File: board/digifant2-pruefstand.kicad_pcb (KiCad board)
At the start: 2 copper layers, 144 x 150 mm, 78 parts, among them J0 VW ECU HARNESS, J1 12V BENCH IN, J2 IDLE VALVE N71, J3 OLED / UI I2C, Q1 2N7002, Q2 P-MOS -30V >=5A, Q3 2N7002, Q5 2N7002, SW1 PUSH, SW2 PUSH, SW3 PUSH, U1 INA226 (0x40), U2 MCP4728 (0x60), U3 INA226 (0x41), U4 AD9833, U5 Raspberry Pi Pico, U6 TS5A3159A, U7 TS5A3159A, U8 TS5A3159A, Y1 25MHz

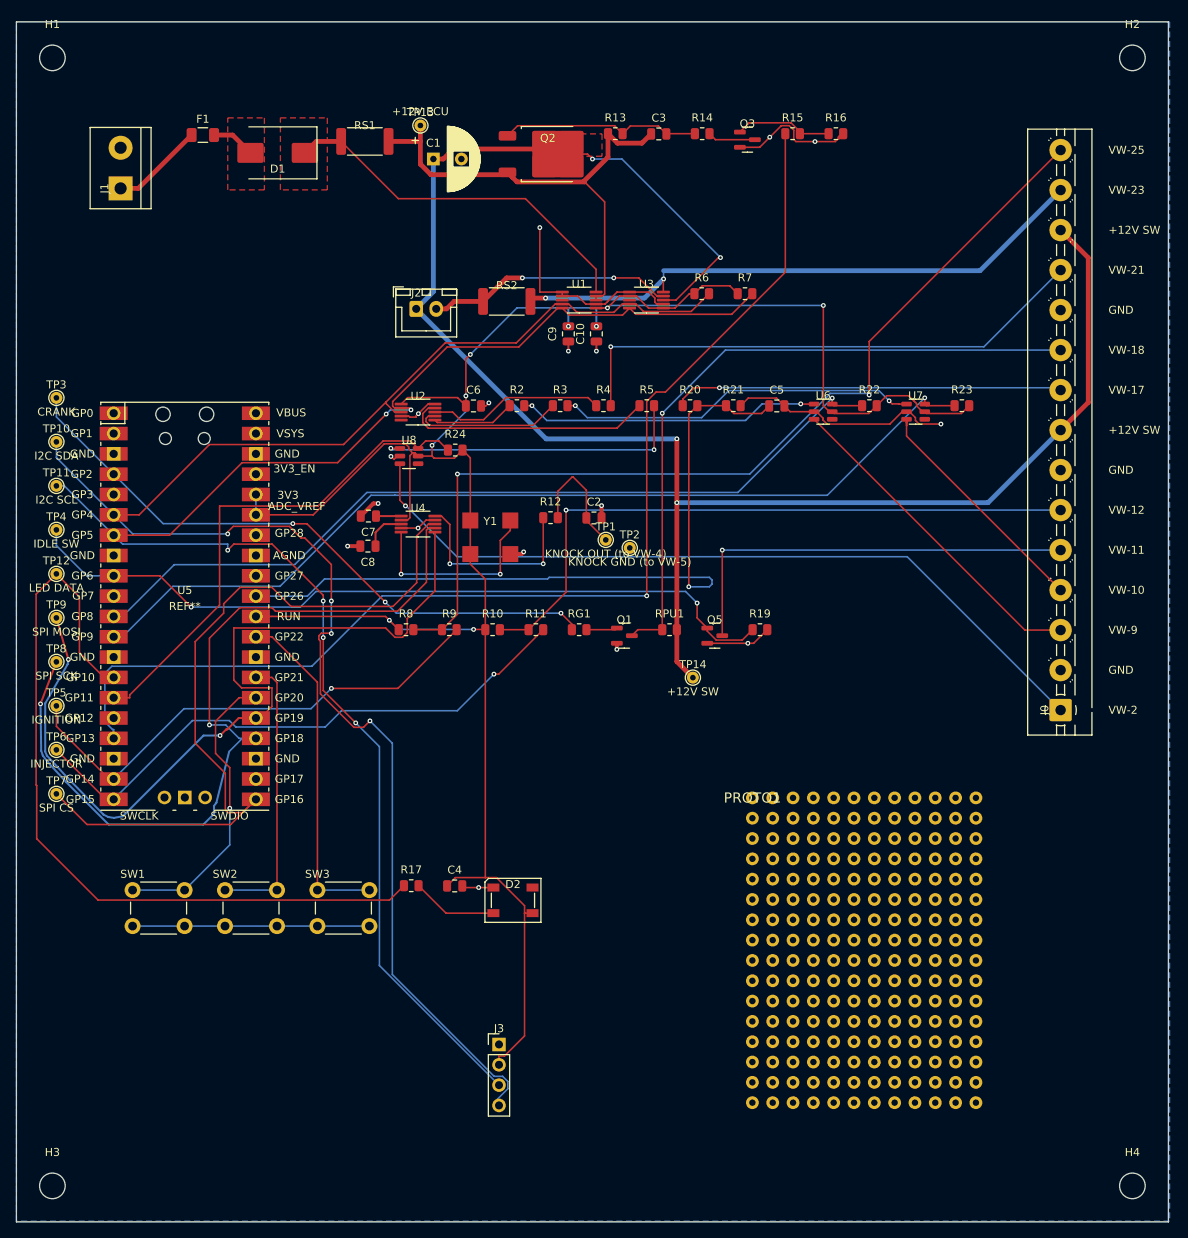
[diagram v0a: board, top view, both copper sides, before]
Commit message: Minor routing touch-ups before ordering from Aisler
Small manual adjustments to Q2_GATE, I2C_SDA/SCL, U4_LOAD, GP10_LED_DATA and
+3V3 traces. DRC unchanged (0 unconnected, only the known cosmetic silkscreen
and footprint-library warnings).

Co-Authored-By: Claude Opus 5.5 <noreply@anthropic.com>
Claude-Session: https://claude.ai/code/session_01XcEuUwwCT37oProAm8HYeY
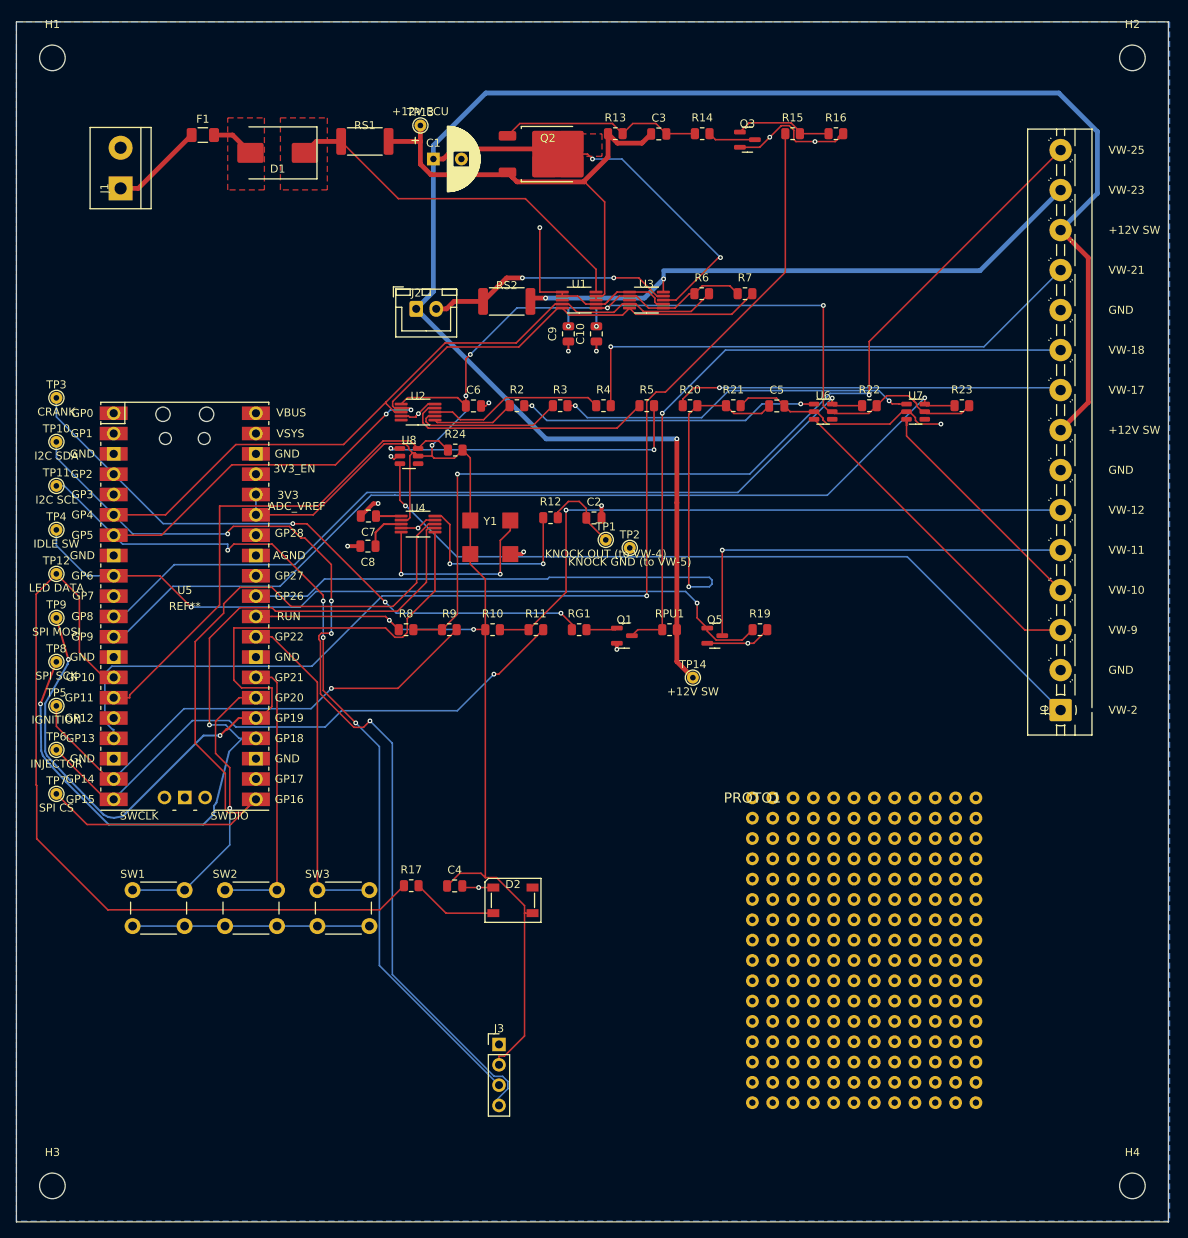
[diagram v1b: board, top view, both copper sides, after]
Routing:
- net +12V_ECU_SW: track 228.7 -> 280.6 mm, vias 4 -> 3
- net U4_LOAD: track 15.5 -> 10.1 mm
- net GP10_LED_DATA: track 100.6 -> 101.6 mm

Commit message: Board: restore pin-1 silk on U6-8, fix J0/J3 labels (from an assembly report)
Found by rendering the actual silkscreen and cross-checking against the
stock footprint and pad positions, via pcbnew scripts (not a full
circuit-synth regeneration, which would discard the hand-routing and
GND pour):

- U6/U7/U8 (TS5A3159A): the stock SOT-23-6 footprint's pin-1 triangle
  was silently dropped when circuit-synth embedded its simplified copy
  into the board. Restored from the stock footprint's geometry.
- J0: per-pin function labels (VW-25, GND, ...) sat on the side the
  harness bundle lies across once wired, unreadable after install.
  Moved to the other side of the connector; one label (+12V SW at pin
  8) shortened and shrunk slightly to clear the R21-R23/U6-U8 row.
- J3: had no per-pin labels at all. Added GND/3V3/SCL/SDA.

All three verified DRC-clean (same pre-existing cosmetic violation
count, zero new) and by rendering the real silkscreen layer before
committing. PCB-level, so only on the next fab run -- DESIGN.md notes
practical workarounds for the board already in hand.

DESIGN.md also documents the Pico 2 socketing approach (the existing
through-hole pads happen to already be at 2.54mm pitch, matching
standard header posts -- no footprint change needed, test-fit first),
the mounting standoffs (holes already exist, just needed BOM entries),
and scopes the schematic-readability complaint as follow-up work (real,
confirmed by rendering it, but risks the circuit-synth hierarchical-
label bugs behind issue #619 if rushed).

Co-Authored-By: Claude Sonnet 5 <noreply@anthropic.com>
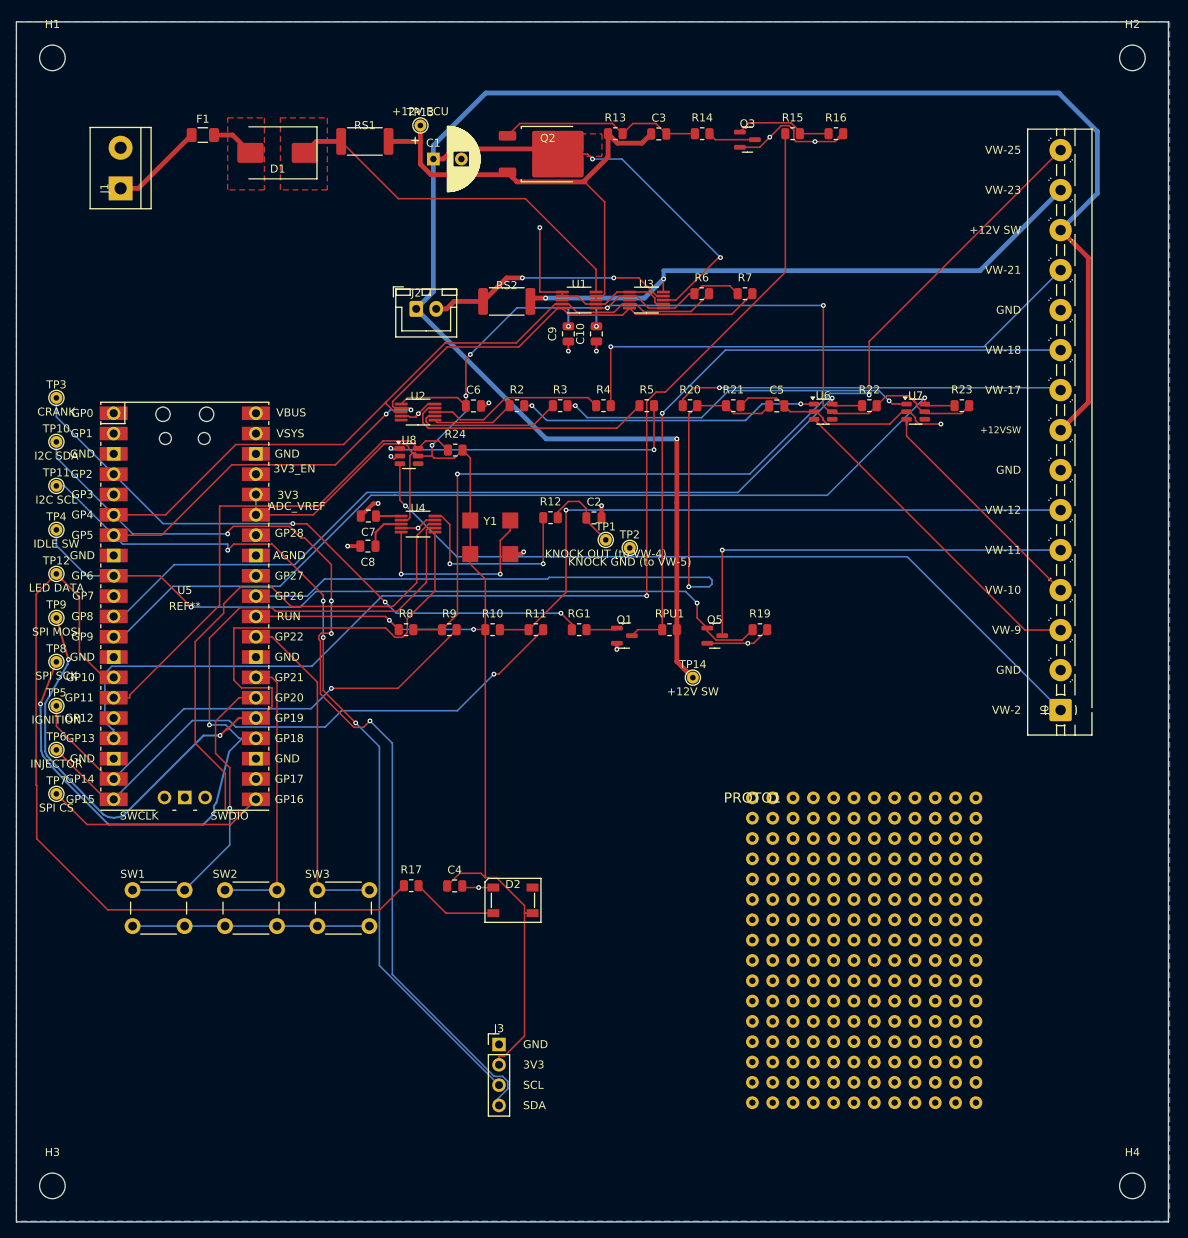
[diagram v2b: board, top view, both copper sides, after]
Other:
- board text added: "+12VSW"
- board text added: "3V3"
- board text added: "SCL"
- board text added: "SDA"
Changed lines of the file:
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@@
 			(layer "F.SilkS")
 		)
+		(fp_poly
+			(pts
+				(xy -1.3 -1.51) (xy -1.54 -1.84) (xy -1.06 -1.84)
+			)
+			(stroke
+				(width 0.15)
+				(type default)
+			)
+			(fill yes)
+			(layer "F.SilkS")
+		)
 		(fp_line
 			(start -2.05 -1.7)
@@
 			(layer "F.SilkS")
 		)
+		(fp_poly
+			(pts
+				(xy -1.3 -1.51) (xy -1.54 -1.84) (xy -1.06 -1.84)
+			)
+			(stroke
+				(width 0.15)
+				(type default)
+			)
+			(fill yes)
+			(layer "F.SilkS")
+		)
 		(fp_line
 			(start -2.05 -1.7)
@@
 			(layer "F.SilkS")
 		)
+		(fp_poly
+			(pts
+				(xy -1.3 -1.51) (xy -1.54 -1.84) (xy -1.06 -1.84)
+			)
+			(stroke
+				(width 0.15)
+				(type default)
+			)
+			(fill yes)
+			(layer "F.SilkS")
+		)
 		(fp_line
 			(start -2.05 -1.7)
@@
 		(layer "Edge.Cuts")
 	)
-	(gr_text "VW-25"
-		(at 136.5 16.025 0)
+	(gr_text "+12VSW"
+		(at 125.6 51.025 0)
 		(layer "F.SilkS")
 		(effects
 			(font
-				(size 1 1)
+				(size 0.85 0.85)
 				(thickness 0.15)
 			)
-			(justify left)
+			(justify right)
 		)
 	)
-	(gr_text "VW-23"
-		(at 136.5 21.025 0)
+	(gr_text "GND"
+		(at 63.325 127.825 0)
 		(layer "F.SilkS")
 		(effects
@@
 		)
 	)
-	(gr_text "+12V SW"
-		(at 136.5 26.025 0)
+	(gr_text "3V3"
+		(at 63.325 130.365 0)
 		(layer "F.SilkS")
 		(effects
@@
 		)
 	)
-	(gr_text "VW-21"
-		(at 136.5 31.025 0)
+	(gr_text "SCL"
+		(at 63.325 132.905 0)
 		(layer "F.SilkS")
 		(effects
@@
 		)
 	)
-	(gr_text "GND"
-		(at 136.5 36.025 0)
+	(gr_text "SDA"
+		(at 63.325 135.445 0)
 		(layer "F.SilkS")
 		(effects
@@
 		)
 	)
-	(gr_text "VW-18"
-		(at 136.5 41.025 0)
+	(gr_text "VW-25"
+		(at 125.6 16.025 0)
 		(layer "F.SilkS")
 		(effects
@@
 				(thickness 0.15)
 			)
-			(justify left)
+			(justify right)
 		)
 	)
-	(gr_text "VW-17"
-		(at 136.5 46.025 0)
+	(gr_text "VW-23"
+		(at 125.6 21.025 0)
 		(layer "F.SilkS")
 		(effects
@@
 				(thickness 0.15)
 			)
-			(justify left)
+			(justify right)
 		)
 	)
 	(gr_text "+12V SW"
-		(at 136.5 51.025 0)
+		(at 125.6 26.025 0)
 		(layer "F.SilkS")
 		(effects
@@
 				(thickness 0.15)
 			)
-			(justify left)
+			(justify right)
+		)
+	)
+	(gr_text "VW-21"
+		(at 125.6 31.025 0)
+		(layer "F.SilkS")
+		(effects
+			(font
+				(size 1 1)
+				(thickness 0.15)
+			)
+			(justify right)
 		)
 	)
 	(gr_text "GND"
-		(at 136.5 56.025 0)
+		(at 125.6 36.025 0)
 		(layer "F.SilkS")
 		(effects
@@
 				(thickness 0.15)
 			)
-			(justify left)
+			(justify right)
+		)
+	)
+	(gr_text "VW-18"
+		(at 125.6 41.025 0)
+		(layer "F.SilkS")
+		(effects
+			(font
+				(size 1 1)
+				(thickness 0.15)
+			)
+			(justify right)
+		)
+	)
+	(gr_text "VW-17"
+		(at 125.6 46.025 0)
+		(layer "F.SilkS")
+		(effects
+			(font
+				(size 1 1)
+				(thickness 0.15)
+			)
+			(justify right)
+		)
+	)
+	(gr_text "GND"
+		(at 125.6 56.025 0)
+		(layer "F.SilkS")
+		(effects
+			(font
+				(size 1 1)
+				(thickness 0.15)
+			)
+			(justify right)
 		)
 	)
 	(gr_text "VW-12"
-		(at 136.5 61.025 0)
+		(at 125.6 61.025 0)
 		(layer "F.SilkS")
 		(effects
@@
 				(thickness 0.15)
 			)
-			(justify left)
+			(justify right)
 		)
 	)
 	(gr_text "VW-11"
-		(at 136.5 66.025 0)
+		(at 125.6 66.025 0)
 		(layer "F.SilkS")
 		(effects
@@
 				(thickness 0.15)
 			)
-			(justify left)
+			(justify right)
 		)
 	)
 	(gr_text "VW-10"
-		(at 136.5 71.025 0)
+		(at 125.6 71.025 0)
 		(layer "F.SilkS")
 		(effects
@@
 				(thickness 0.15)
 			)
-			(justify left)
+			(justify right)
 		)
 	)
 	(gr_text "VW-9"
-		(at 136.5 76.025 0)
+		(at 125.6 76.025 0)
 		(layer "F.SilkS")
 		(effects
@@
 				(thickness 0.15)
 			)
-			(justify left)
+			(justify right)
 		)
 	)
 	(gr_text "GND"
-		(at 136.5 81.025 0)
+		(at 125.6 81.025 0)
 		(layer "F.SilkS")
 		(effects
@@
 				(thickness 0.15)
 			)
-			(justify left)
+			(justify right)
 		)
 	)
 	(gr_text "VW-2"
-		(at 136.5 86.025 0)
+		(at 125.6 86.025 0)
 		(layer "F.SilkS")
 		(effects
@@
 				(thickness 0.15)
 			)
-			(justify left)
+			(justify right)
 		)
 	)
